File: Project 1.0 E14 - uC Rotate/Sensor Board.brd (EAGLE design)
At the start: 40 x 75 mm, 93 parts, among them IC1 LT1963EST-1.5, IC2 LT1963EST-1.5, IC4 LT1963EST-1.5

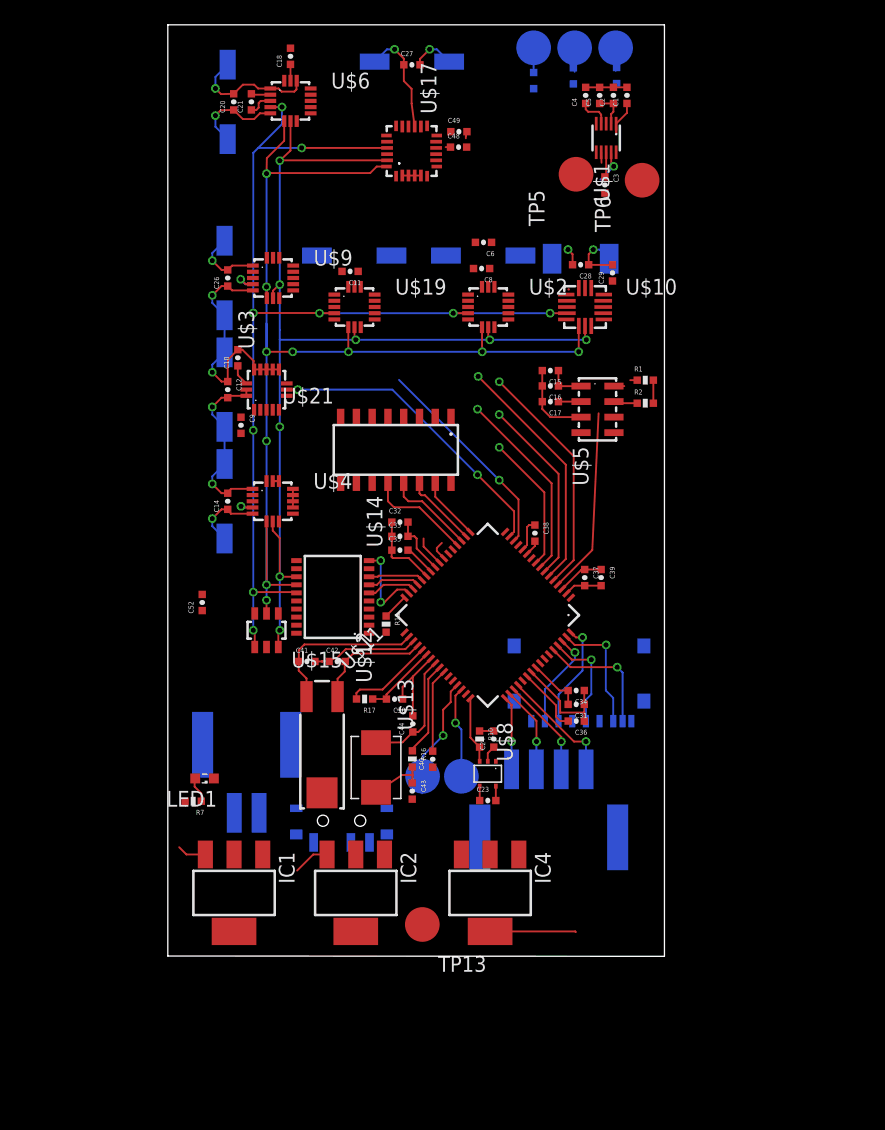
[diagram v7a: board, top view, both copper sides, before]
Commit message: All signal connections have been completed. Space has been adequately left between traces to allow for GND plane fill in. Power and GND have not been connected and signal and power trace widths have not been finalised. LSM9DS0 interrupts have not been finalised and may have been incorrectly connected.  LSM9DS0 Gyroscope data enable pin has not been connected since currently it is not clear what its use is or how it is to be used. Gyroscope programmable interrupt pin has been connected but the desired connection may be the gyroscope data ready pin. Also currently there appears to be no interrupt for the magnetometer and this will need to be fixed to enable all 9 axis to be fully used.
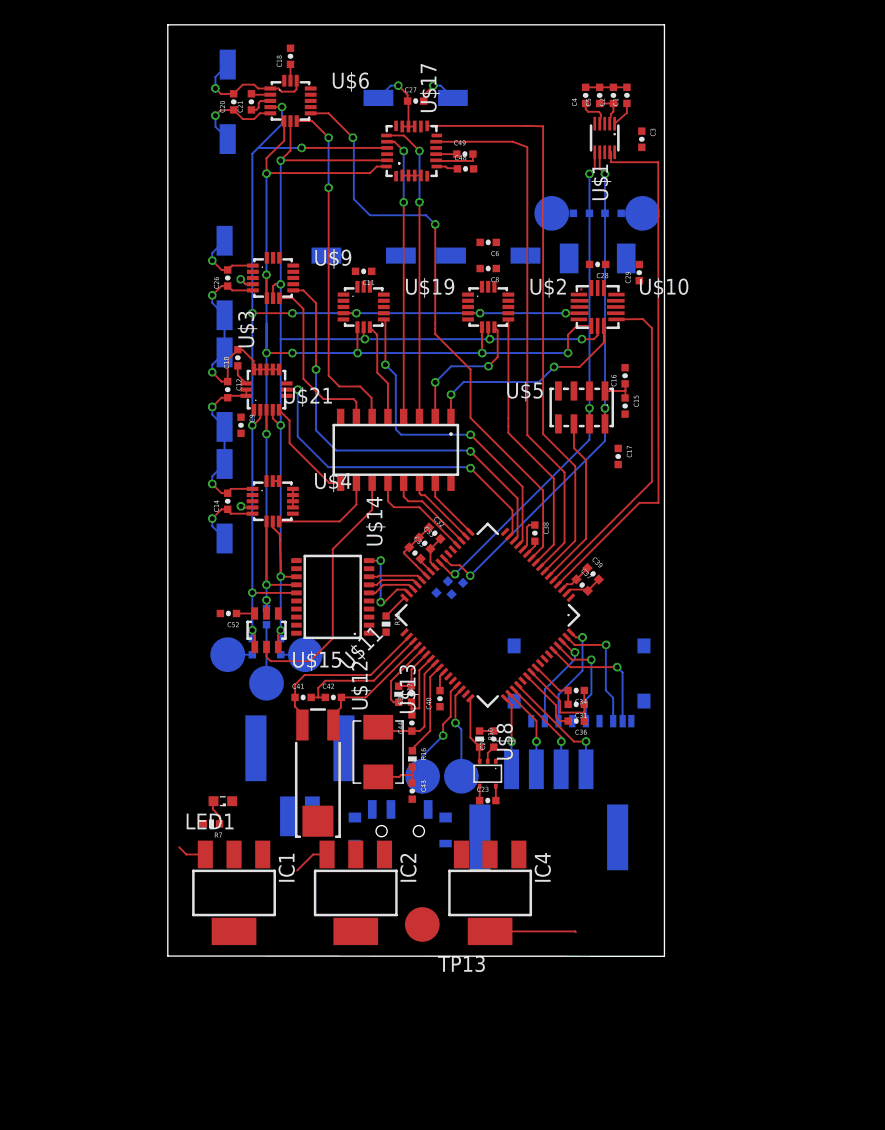
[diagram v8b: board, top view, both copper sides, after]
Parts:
- added R5, R8: 0, Kas-Passives:0402-RES
- TP5, TP6: device Kas-Passives:TESTPAD(ROUND) -> Kas-Connectors:TESTPAD(ROUND)
- moved TP2 56.9 mm to (7.95, 22.0), turned to 270 degrees
- moved TP3 54.9 mm to (11.1, 24.3), turned to 270 degrees
- moved TP1 54.7 mm to (4.83, 24.3), turned to 270 degrees
- moved R6 53.4 mm to (9.09, 24.9), turned to 270 degrees
- moved R3 50.9 mm to (6.81, 24.9), turned to 270 degrees
- moved R4 50.1 mm to (7.95, 27.3), turned to 270 degrees
- moved R1 22.6 mm to (23.3, 29.6), flipped to the bottom, turned to 315 degrees
- moved R2 22.1 mm to (22.1, 29.7), flipped to the bottom, turned to 315 degrees
- moved C17 7.03 mm to (36.3, 40.2), turned to 270 degrees
- moved C15 6.66 mm to (36.8, 44.3), turned to 270 degrees
- moved C16 6.08 mm to (36.8, 46.7), turned to 90 degrees
- moved C40 4.91 mm to (21.9, 20.7)
- moved S1 4.80 mm to (18.7, 10.1), turned to 180 degrees
- moved C3 4.73 mm to (38.2, 65.8)
- moved U$16 4.30 mm to (10.6, 19.4)
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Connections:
- new net N$24: R5.2, TP6.P$1
- new net N$26: R8.2, TP5.P$1
- net CS-LSM9D30-G: now also U$21.P$3; no longer U$21.P$4
- net CS-LSM9DS0-XM: now also U$21.P$4; no longer U$21.P$3
- net INT1-MAG3110: now also U$11.P$4; no longer U$11.P$5
- net INT1-MPL311: now also U$11.P$6; no longer U$11.P$4
- net INT2-ADXL362: now also U$11.P$5; no longer U$11.P$8
- net INT2-H3LIS331: now also U$11.P$9; no longer U$11.P$10
- net INT2-LSM303: now also U$11.P$10; no longer U$11.P$7
- net INT2-MAX21000: now also U$11.P$13; no longer U$11.P$6
- net LSM9D-INT-G: now also U$11.P$8; no longer U$11.P$9
- net LSM9D-INT1-XM: now also U$11.P$7; no longer U$11.P$13
- net SCL-0: now also R5.1; no longer TP6.P$1
- net SDA-0: now also R8.1; no longer TP5.P$1
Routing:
- net LSM9D-INT1-XM: track 0.00 -> 47.3 mm
- net SCL-0: track 3.90 -> 42.7 mm, vias 0 -> 3
- net SDA-0: track 4.37 -> 41.5 mm, vias 0 -> 3
- net INT2-LSM303: track 15.1 -> 47.5 mm, vias 1 -> 2
- net LSM9D-INT-G: track 11.1 -> 43.3 mm, vias 1 -> 0
- net CS-LSM303: track 0.48 -> 28.5 mm, vias 0 -> 2
- net CS-LSM9D30-G: track 0.00 -> 24.6 mm, vias 0 -> 2
- net CS-LSM9DS0-XM: track 0.00 -> 23.0 mm, vias 0 -> 2
- net INT2-H3LIS331: track 0.00 -> 21.7 mm
- net INT1-MAG3110: track 22.0 -> 43.1 mm, vias 2 -> 0
- net CS-ADT7301: track 0.00 -> 20.9 mm
- net 3.3V: track 82.6 -> 63.9 mm, vias 6 -> 5
- net INT2-LIS3DH: track 17.3 -> 34.8 mm, vias 1 -> 2
- net CS-ADXL362: track 0.00 -> 17.2 mm, vias 0 -> 2
- net CS-LIS3DH: track 0.00 -> 14.2 mm
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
